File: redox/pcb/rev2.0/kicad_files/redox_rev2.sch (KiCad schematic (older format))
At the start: 144 parts, among them J1 AVR-ISP-6, J2 OLED-SSD1306, K1 KEYSW, K10 KEYSW, K11 KEYSW, K12 KEYSW, K13 KEYSW, K14 KEYSW, K15 KEYSW, K16 KEYSW, K17 KEYSW, K18 KEYSW, K19 KEYSW, K2 KEYSW, K20 KEYSW, K21 KEYSW, K22 KEYSW, K23 KEYSW, K24 KEYSW, K25 KEYSW, K26 KEYSW, K27 KEYSW, K28 KEYSW, K29 KEYSW, K3 KEYSW, K30 KEYSW, K31 KEYSW, K32 KEYSW, K33 KEYSW, K34 KEYSW, K35 KEYSW, K4 KEYSW, K5 KEYSW, K6 KEYSW, K7 KEYSW, K8 KEYSW, K9 KEYSW, Q1 2N7002, U1 PRTR5V0U2X, U2 ATmega32U4, Y1 16Mhz

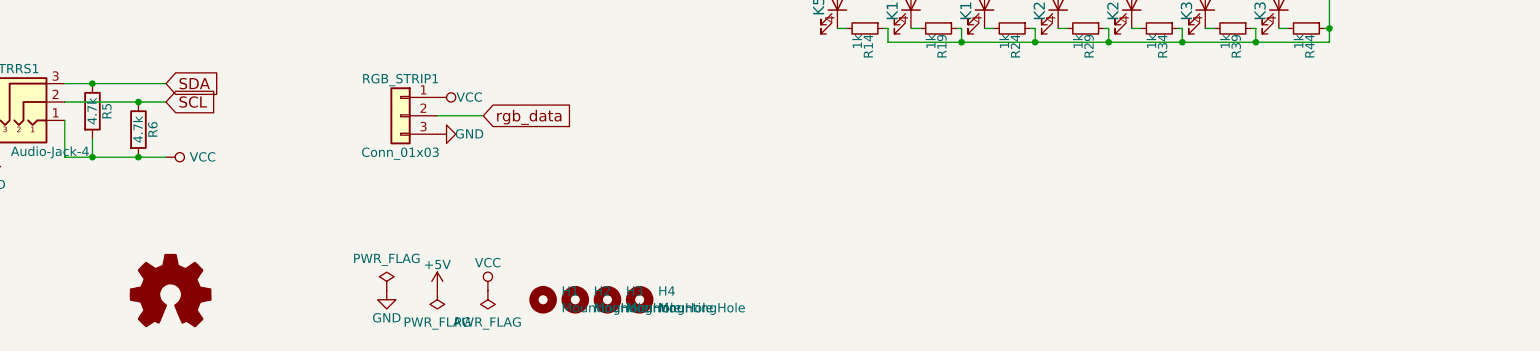
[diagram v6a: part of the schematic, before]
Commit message: Add holes for OLED cover and moove mounting holes
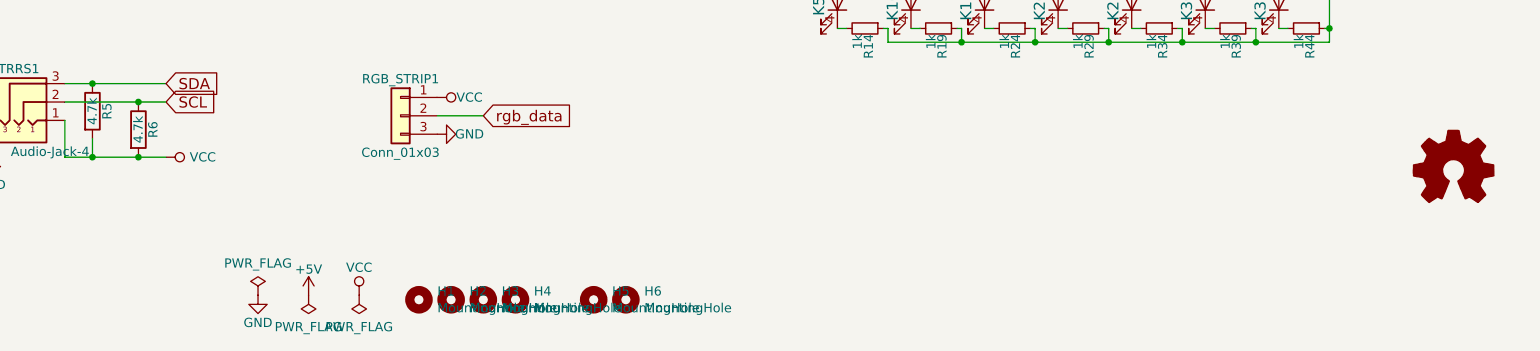
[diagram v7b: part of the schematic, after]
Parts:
- added H5, H6: MountingHole, redox_footprints:HOLE_M2, symbol Mechanical:MountingHole
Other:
- moved on the sheet: H1, H2, H3, H4
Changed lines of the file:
@@
 L Mechanical:MountingHole H1
 U 1 1 5EB1BFE2
-P 5775 7550
-F 0 "H1" H 5875 7596 50  0000 L CNN
-F 1 "MountingHole" H 5875 7505 50  0000 L CNN
-F 2 "redox_footprints:HOLE_M3" H 5775 7550 50  0001 C CNN
-F 3 "~" H 5775 7550 50  0001 C CNN
-	1    5775 7550
+P 5100 7550
+F 0 "H1" H 5200 7596 50  0000 L CNN
+F 1 "MountingHole" H 5200 7505 50  0000 L CNN
+F 2 "redox_footprints:HOLE_M3" H 5100 7550 50  0001 C CNN
+F 3 "~" H 5100 7550 50  0001 C CNN
+	1    5100 7550
 	1    0    0    -1
 $EndComp
@@
 L Mechanical:MountingHole H2
 U 1 1 5EB1C731
-P 5950 7550
-F 0 "H2" H 6050 7596 50  0000 L CNN
-F 1 "MountingHole" H 6050 7505 50  0000 L CNN
-F 2 "redox_footprints:HOLE_M3" H 5950 7550 50  0001 C CNN
-F 3 "~" H 5950 7550 50  0001 C CNN
-	1    5950 7550
+P 5275 7550
+F 0 "H2" H 5375 7596 50  0000 L CNN
+F 1 "MountingHole" H 5375 7505 50  0000 L CNN
+F 2 "redox_footprints:HOLE_M3" H 5275 7550 50  0001 C CNN
+F 3 "~" H 5275 7550 50  0001 C CNN
+	1    5275 7550
 	1    0    0    -1
 $EndComp
@@
 L Mechanical:MountingHole H3
 U 1 1 5EB1CBBB
-P 6125 7550
-F 0 "H3" H 6225 7596 50  0000 L CNN
-F 1 "MountingHole" H 6225 7505 50  0000 L CNN
-F 2 "redox_footprints:HOLE_M3" H 6125 7550 50  0001 C CNN
-F 3 "~" H 6125 7550 50  0001 C CNN
-	1    6125 7550
+P 5450 7550
+F 0 "H3" H 5550 7596 50  0000 L CNN
+F 1 "MountingHole" H 5550 7505 50  0000 L CNN
+F 2 "redox_footprints:HOLE_M3" H 5450 7550 50  0001 C CNN
+F 3 "~" H 5450 7550 50  0001 C CNN
+	1    5450 7550
 	1    0    0    -1
 $EndComp
@@
 L Mechanical:MountingHole H4
 U 1 1 5EB1D004
-P 6300 7550
-F 0 "H4" H 6400 7596 50  0000 L CNN
-F 1 "MountingHole" H 6400 7505 50  0000 L CNN
-F 2 "redox_footprints:HOLE_M3" H 6300 7550 50  0001 C CNN
-F 3 "~" H 6300 7550 50  0001 C CNN
-	1    6300 7550
+P 5625 7550
+F 0 "H4" H 5725 7596 50  0000 L CNN
+F 1 "MountingHole" H 5725 7505 50  0000 L CNN
+F 2 "redox_footprints:HOLE_M3" H 5625 7550 50  0001 C CNN
+F 3 "~" H 5625 7550 50  0001 C CNN
+	1    5625 7550
 	1    0    0    -1
 $EndComp
@@
 L power:PWR_FLAG #FLG0101
 U 1 1 5F8050DA
-P 4925 7500
-F 0 "#FLG0101" H 4925 7575 50  0001 C CNN
-F 1 "PWR_FLAG" H 4925 7673 50  0000 C CNN
-F 2 "" H 4925 7500 50  0001 C CNN
-F 3 "~" H 4925 7500 50  0001 C CNN
-	1    4925 7500
+P 4225 7525
+F 0 "#FLG0101" H 4225 7600 50  0001 C CNN
+F 1 "PWR_FLAG" H 4225 7698 50  0000 C CNN
+F 2 "" H 4225 7525 50  0001 C CNN
+F 3 "~" H 4225 7525 50  0001 C CNN
+	1    4225 7525
 	1    0    0    -1
 $EndComp
@@
 L power:PWR_FLAG #FLG0102
 U 1 1 5F805F05
-P 5200 7500
-F 0 "#FLG0102" H 5200 7575 50  0001 C CNN
-F 1 "PWR_FLAG" H 5200 7673 50  0000 C CNN
-F 2 "" H 5200 7500 50  0001 C CNN
-F 3 "~" H 5200 7500 50  0001 C CNN
-	1    5200 7500
+P 4500 7525
+F 0 "#FLG0102" H 4500 7600 50  0001 C CNN
+F 1 "PWR_FLAG" H 4500 7698 50  0000 C CNN
+F 2 "" H 4500 7525 50  0001 C CNN
+F 3 "~" H 4500 7525 50  0001 C CNN
+	1    4500 7525
 	-1   0    0    1
 $EndComp
@@
 L power:PWR_FLAG #FLG0103
 U 1 1 5F807001
-P 5475 7500
-F 0 "#FLG0103" H 5475 7575 50  0001 C CNN
-F 1 "PWR_FLAG" H 5475 7673 50  0000 C CNN
-F 2 "" H 5475 7500 50  0001 C CNN
-F 3 "~" H 5475 7500 50  0001 C CNN
-	1    5475 7500
+P 4775 7525
+F 0 "#FLG0103" H 4775 7600 50  0001 C CNN
+F 1 "PWR_FLAG" H 4775 7698 50  0000 C CNN
+F 2 "" H 4775 7525 50  0001 C CNN
+F 3 "~" H 4775 7525 50  0001 C CNN
+	1    4775 7525
 	-1   0    0    1
 $EndComp
@@
 L power:GND #PWR?
 U 1 1 5F807F2D
-P 4925 7500
+P 4225 7525
 AR Path="/5EAF3E37/5F807F2D" Ref="#PWR?"  Part="1"
 AR Path="/5F807F2D" Ref="#PWR0102"  Part="1"
-F 0 "#PWR0102" H 4925 7250 50  0001 C CNN
-F 1 "GND" H 4925 7350 50  0000 C CNN
-F 2 "" H 4925 7500 50  0001 C CNN
-F 3 "" H 4925 7500 50  0001 C CNN
-	1    4925 7500
+F 0 "#PWR0102" H 4225 7275 50  0001 C CNN
+F 1 "GND" H 4225 7375 50  0000 C CNN
+F 2 "" H 4225 7525 50  0001 C CNN
+F 3 "" H 4225 7525 50  0001 C CNN
+	1    4225 7525
 	1    0    0    -1
 $EndComp
@@
 L power:+5V #PWR?
 U 1 1 5F808756
-P 5200 7500
+P 4500 7525
 AR Path="/5EAF3E37/5F808756" Ref="#PWR?"  Part="1"
 AR Path="/5F808756" Ref="#PWR0103"  Part="1"
-F 0 "#PWR0103" H 5200 7350 50  0001 C CNN
-F 1 "+5V" H 5200 7640 50  0000 C CNN
-F 2 "" H 5200 7500 50  0001 C CNN
-F 3 "" H 5200 7500 50  0001 C CNN
-	1    5200 7500
+F 0 "#PWR0103" H 4500 7375 50  0001 C CNN
+F 1 "+5V" H 4500 7665 50  0000 C CNN
+F 2 "" H 4500 7525 50  0001 C CNN
+F 3 "" H 4500 7525 50  0001 C CNN
+	1    4500 7525
 	1    0    0    -1
 $EndComp
@@
 L power:VCC #PWR?
 U 1 1 5F846CA1
-P 5475 7500
+P 4775 7525
 AR Path="/5EAF3E37/5F846CA1" Ref="#PWR?"  Part="1"
 AR Path="/5F846CA1" Ref="#PWR0104"  Part="1"
-F 0 "#PWR0104" H 5475 7350 50  0001 C CNN
-F 1 "VCC" H 5475 7650 50  0000 C CNN
-F 2 "" H 5475 7500 50  0001 C CNN
-F 3 "" H 5475 7500 50  0001 C CNN
-	1    5475 7500
+F 0 "#PWR0104" H 4775 7375 50  0001 C CNN
+F 1 "VCC" H 4775 7675 50  0000 C CNN
+F 2 "" H 4775 7525 50  0001 C CNN
+F 3 "" H 4775 7525 50  0001 C CNN
+	1    4775 7525
 	1    0    0    -1
 $EndComp
@@
 L Graphic:Logo_Open_Hardware_Small #LOGO1
 U 1 1 6041354B
-P 3750 7525
-F 0 "#LOGO1" H 3750 7800 50  0001 C CNN
-F 1 "Logo_Open_Hardware_Small" H 3750 7300 50  0001 C CNN
-F 2 "" H 3750 7525 50  0001 C CNN
-F 3 "~" H 3750 7525 50  0001 C CNN
-	1    3750 7525
-	1    0    0    -1
-$EndComp
+P 10725 6850
+F 0 "#LOGO1" H 10725 7125 50  0001 C CNN
+F 1 "Logo_Open_Hardware_Small" H 10725 6625 50  0001 C CNN
+F 2 "" H 10725 6850 50  0001 C CNN
+F 3 "~" H 10725 6850 50  0001 C CNN
+	1    10725 6850
+	1    0    0    -1
+$EndComp
+$Comp
+L Mechanical:MountingHole H5
+U 1 1 5ED447DA
+P 6050 7550
+F 0 "H5" H 6150 7596 50  0000 L CNN
+F 1 "MountingHole" H 6150 7505 50  0000 L CNN
+F 2 "redox_footprints:HOLE_M2" H 6050 7550 50  0001 C CNN
+F 3 "~" H 6050 7550 50  0001 C CNN
+	1    6050 7550
+	1    0    0    -1
+$EndComp
+$Comp
+L Mechanical:MountingHole H6
+U 1 1 5ED44D0D
+P 6225 7550
+F 0 "H6" H 6325 7596 50  0000 L CNN
+F 1 "MountingHole" H 6325 7505 50  0000 L CNN
+F 2 "redox_footprints:HOLE_M2" H 6225 7550 50  0001 C CNN
+F 3 "~" H 6225 7550 50  0001 C CNN
+	1    6225 7550
+	1    0    0    -1
+$EndComp

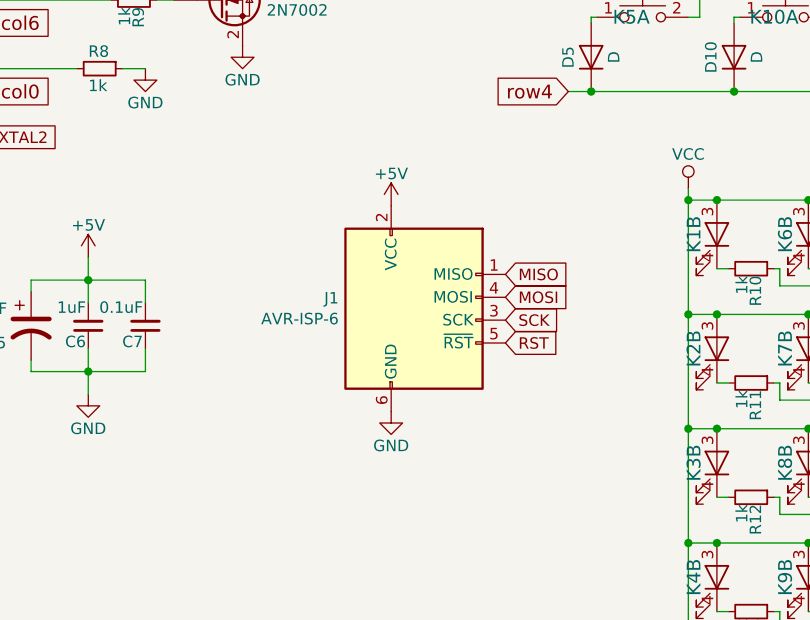
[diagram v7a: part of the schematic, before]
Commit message: Move mounting holes to be compliant with redox rev1
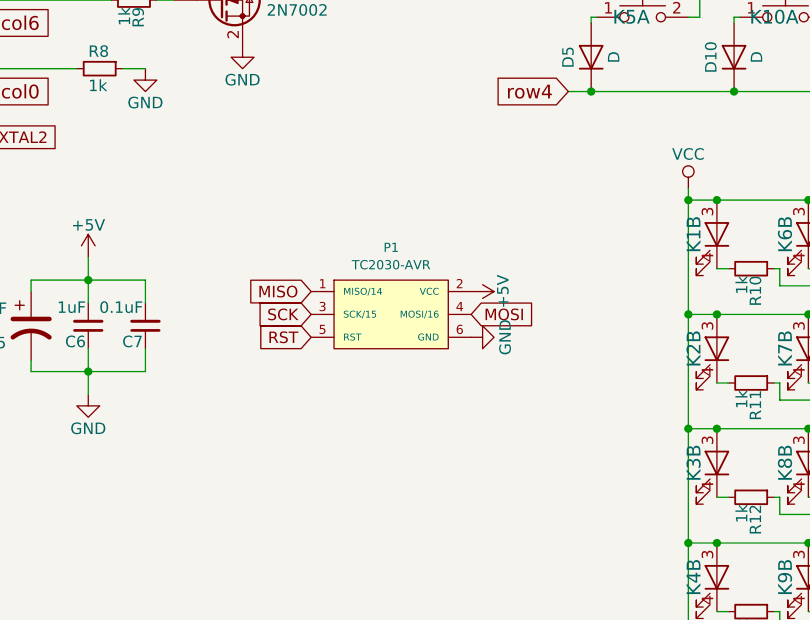
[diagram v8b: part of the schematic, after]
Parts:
- removed J1: AVR-ISP-6, Connector_PinHeader_2.54mm:PinHeader_2x03_P2.54mm_Vertical, symbol Connector:AVR-ISP-6
- added P1: TC2030-AVR, Connector_PinHeader_2.54mm:PinHeader_2x03_P2.54mm_Vertical, symbol keebio:TC2030-AVR
- H5, H6: footprint redox_footprints:HOLE_M2 -> redox_footprints:M2_HOLE_PCB
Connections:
- net +5V: now also P1.2 (VCC)
- net GND: now also P1.6 (GND)
- net MISO: now also P1.1 (MISO/14)
- net MOSI: now also P1.4 (MOSI/16)
- net RST: now also P1.5 (RST)
- net SCK: now also P1.3 (SCK/15)
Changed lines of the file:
@@
 	900  1350 1025 1350
-$Comp
-L Connector:AVR-ISP-6 J1
-U 1 1 5ECF58F1
-P 6050 4325
-F 0 "J1" H 5721 4421 50  0000 R CNN
-F 1 "AVR-ISP-6" H 5721 4330 50  0000 R CNN
-F 2 "Connector_PinHeader_2.54mm:PinHeader_2x03_P2.54mm_Vertical" V 5800 4375 50  0001 C CNN
-F 3 " ~" H 4775 3775 50  0001 C CNN
-	1    6050 4325
-	1    0    0    -1
-$EndComp
 $Comp
 L power:GND #PWR?
 U 1 1 5ECF6FCC
-P 5950 4725
+P 6300 4400
 AR Path="/5EAF3E37/5ECF6FCC" Ref="#PWR?"  Part="1"
 AR Path="/5ECF6FCC" Ref="#PWR020"  Part="1"
-F 0 "#PWR020" H 5950 4475 50  0001 C CNN
-F 1 "GND" H 5950 4575 50  0000 C CNN
-F 2 "" H 5950 4725 50  0001 C CNN
-F 3 "" H 5950 4725 50  0001 C CNN
-	1    5950 4725
-	1    0    0    -1
+F 0 "#PWR020" H 6300 4150 50  0001 C CNN
+F 1 "GND" H 6300 4250 50  0000 C CNN
+F 2 "" H 6300 4400 50  0001 C CNN
+F 3 "" H 6300 4400 50  0001 C CNN
+	1    6300 4400
+	0    -1   -1   0
 $EndComp
 $Comp
 L power:+5V #PWR?
 U 1 1 5ECF83AB
-P 5950 3825
+P 6300 4200
 AR Path="/5EAF3E37/5ECF83AB" Ref="#PWR?"  Part="1"
 AR Path="/5ECF83AB" Ref="#PWR019"  Part="1"
-F 0 "#PWR019" H 5950 3675 50  0001 C CNN
-F 1 "+5V" H 5950 3965 50  0000 C CNN
-F 2 "" H 5950 3825 50  0001 C CNN
-F 3 "" H 5950 3825 50  0001 C CNN
-	1    5950 3825
-	1    0    0    -1
+F 0 "#PWR019" H 6300 4050 50  0001 C CNN
+F 1 "+5V" H 6300 4340 50  0000 C CNN
+F 2 "" H 6300 4200 50  0001 C CNN
+F 3 "" H 6300 4200 50  0001 C CNN
+	1    6300 4200
+	0    1    1    0
 $EndComp
 Text GLabel 4175 1325 2    50   Input ~ 0
@@
 Text GLabel 4175 1425 2    50   Input ~ 0
 MISO
-Text GLabel 6450 4225 2    50   Input ~ 0
+Text GLabel 6300 4300 2    50   Input ~ 0
 MOSI
-Text GLabel 6450 4125 2    50   Input ~ 0
+Text GLabel 5600 4200 0    50   Input ~ 0
 MISO
 Text GLabel 4175 1225 2    50   Input ~ 0
 SCK
-Text GLabel 6450 4325 2    50   Input ~ 0
+Text GLabel 5600 4300 0    50   Input ~ 0
 SCK
 Text GLabel 1800 1350 2    50   Input ~ 0
@@
 Wire Wire Line
 	1725 1350 1800 1350
-Text GLabel 6450 4425 2    50   Input ~ 0
+Text GLabel 5600 4400 0    50   Input ~ 0
 RST
 $Comp
@@
 F 0 "H5" H 6150 7596 50  0000 L CNN
 F 1 "MountingHole" H 6150 7505 50  0000 L CNN
-F 2 "redox_footprints:HOLE_M2" H 6050 7550 50  0001 C CNN
+F 2 "redox_footprints:M2_HOLE_PCB" H 6050 7550 50  0001 C CNN
 F 3 "~" H 6050 7550 50  0001 C CNN
 	1    6050 7550
@@
 F 0 "H6" H 6325 7596 50  0000 L CNN
 F 1 "MountingHole" H 6325 7505 50  0000 L CNN
-F 2 "redox_footprints:HOLE_M2" H 6225 7550 50  0001 C CNN
+F 2 "redox_footprints:M2_HOLE_PCB" H 6225 7550 50  0001 C CNN
 F 3 "~" H 6225 7550 50  0001 C CNN
 	1    6225 7550
 	1    0    0    -1
 $EndComp
+$Comp
+L keebio:TC2030-AVR P1
+U 1 1 5EE96AE2
+P 5950 4300
+F 0 "P1" H 5950 4592 40  0000 C CNN
+F 1 "TC2030-AVR" H 5950 4516 40  0000 C CNN
+F 2 "Connector_PinHeader_2.54mm:PinHeader_2x03_P2.54mm_Vertical" H 5950 4300 50  0001 C CNN
+F 3 "" H 5950 4300 50  0001 C CNN
+	1    5950 4300
+	1    0    0    -1
+$EndComp
